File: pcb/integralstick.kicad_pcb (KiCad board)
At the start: 4 copper layers, 231 parts, among them J1 CONN_INTEGRALSTICK_FPGA_DEVICE, J2 CONN_INTEGRALSTICK_MCU_DEVICE, Q1 SSM6N58NU, Q2 SSM6N58NU, Q3 SSM6N58NU, U1 STM32F777NIH6‎, U10 DSC6083MI2A-032K768, U12 DSC6001HI2A-025.0000‎, U2 XC7A50T-1FTG256C, U3 S27KS0641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

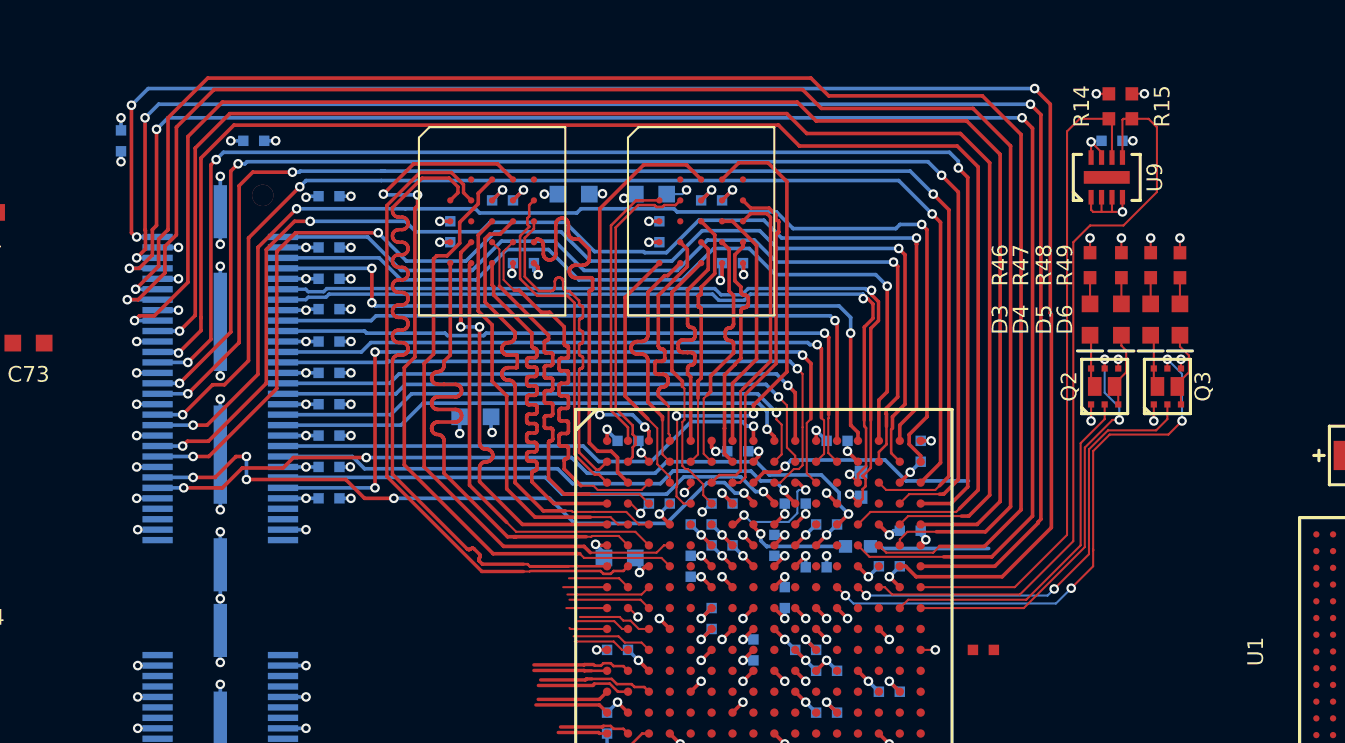
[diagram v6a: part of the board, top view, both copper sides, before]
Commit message: More efficient use of top right area above FPGA
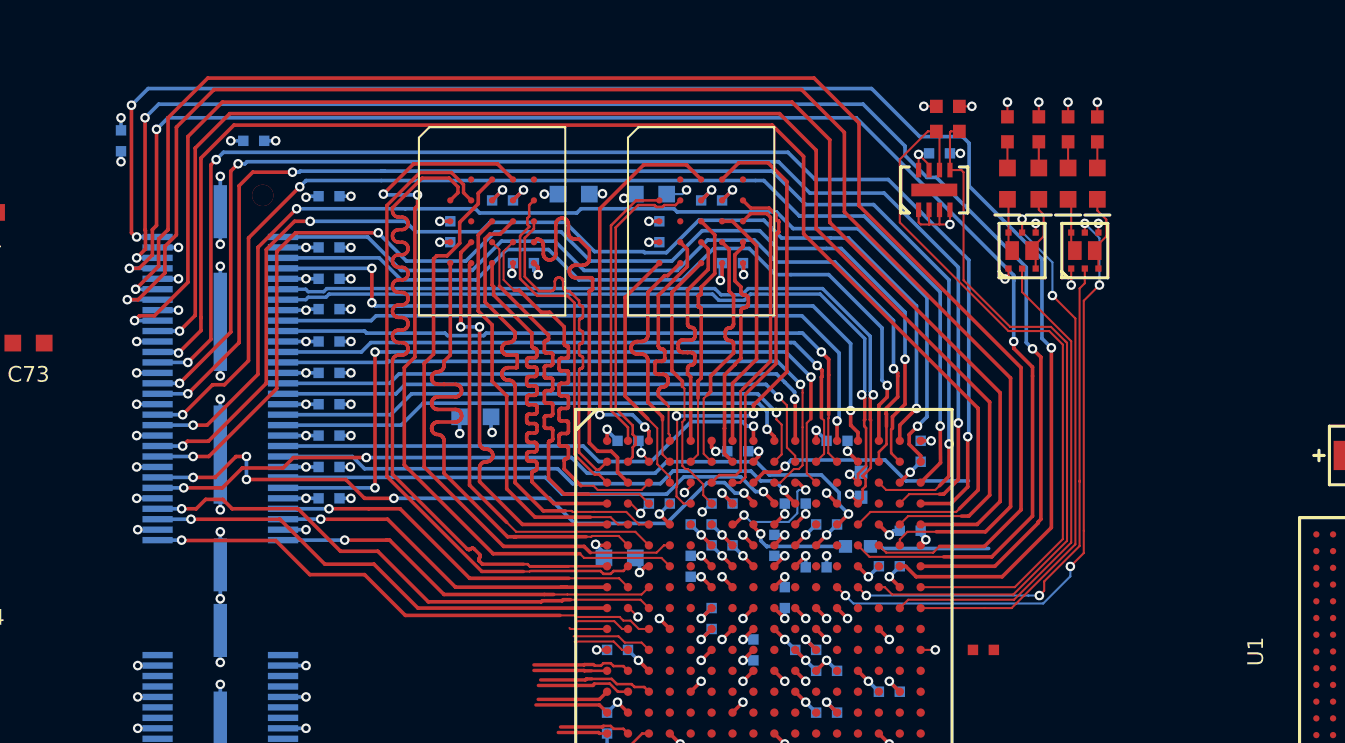
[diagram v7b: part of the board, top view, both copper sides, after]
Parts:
- moved C44 8.27 mm to (72.4, 21.8)
- moved R14 8.27 mm to (72.2, 20.1)
- moved R15 8.27 mm to (73.3, 20.1)
- moved U9 8.27 mm to (72.2, 23.5)
- moved D5 7.61 mm to (78.5, 23.2)
- moved D6 7.61 mm to (80.0, 23.2)
- moved Q2 7.61 mm to (76.3, 26.4)
- moved Q3 7.61 mm to (79.3, 26.4)
- moved R48 7.61 mm to (78.5, 20.6)
- moved R49 7.61 mm to (80.0, 20.6)
- moved D3 7.61 mm to (75.7, 23.2)
- moved D4 7.61 mm to (77.2, 23.2)
- moved R46 7.61 mm to (75.7, 20.6)
- moved R47 7.61 mm to (77.2, 20.6)
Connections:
- U2 pad E5: /RAM/GPIO_1V8_0 -> /RAM/GPIO_1V8_9
- U2 pad E6: /RAM/GPIO_1V8_1 -> /RAM/GPIO_1V8_7
- U2 pad G5: /RAM/GPIO_1V8_2 -> /RAM/GPIO_1V8_12
- U2 pad H1: /RAM/GPIO_1V8_8 -> /RAM/GPIO_1V8_3
- U2 pad H2: /RAM/GPIO_1V8_7 -> /RAM/GPIO_1V8_1
- U2 pad H3: /RAM/GPIO_1V8_10 -> /RAM/GPIO_1V8_5
- U2 pad H4: /RAM/GPIO_1V8_4 -> /RAM/GPIO_1V8_15
- U2 pad H5: /RAM/GPIO_1V8_3 -> /RAM/GPIO_1V8_8
- U2 pad J1: /RAM/GPIO_1V8_12 -> /RAM/GPIO_1V8_2
- U2 pad J3: /RAM/GPIO_1V8_9 -> /RAM/GPIO_1V8_0
- U2 pad J5: /RAM/GPIO_1V8_5 -> /RAM/GPIO_1V8_10
- U2 pad K3: /RAM/GPIO_1V8_15 -> /RAM/GPIO_1V8_4
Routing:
- net /RAM/GPIO_1V8_0: track 0.00 -> 26.0 mm, vias 0 -> 1
- net /RAM/GPIO_1V8_4: track 0.00 -> 25.3 mm, vias 0 -> 1
- net /RAM/GPIO_1V8_2: track 0.00 -> 23.3 mm, vias 0 -> 1
- net /RAM/GPIO_1V8_5: track 0.00 -> 18.7 mm, vias 0 -> 1
- net /RAM/GPIO_1V8_1: track 0.00 -> 18.1 mm, vias 0 -> 1
- net /RAM/GPIO_1V8_3: track 0.00 -> 17.1 mm, vias 0 -> 1
- net /FPGA/GPIO_LED0: track 17.1 -> 23.6 mm
- net /FPGA/GPIO_LED1: track 19.6 -> 25.9 mm
- net /FPGA/IO_3V3_25: track 79.1 -> 74.4 mm
- net /FPGA/IO_3V3_17: track 71.3 -> 66.7 mm
- net /FPGA/IO_3V3_19: track 70.5 -> 66.0 mm
- net /FPGA/IO_3V3_27: track 77.3 -> 72.8 mm
- net /FPGA/IO_3V3_21: track 72.8 -> 68.4 mm
- net /FPGA/IO_3V3_22: track 76.2 -> 71.9 mm
- net /FPGA/IO_3V3_23: track 78.3 -> 74.1 mm
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
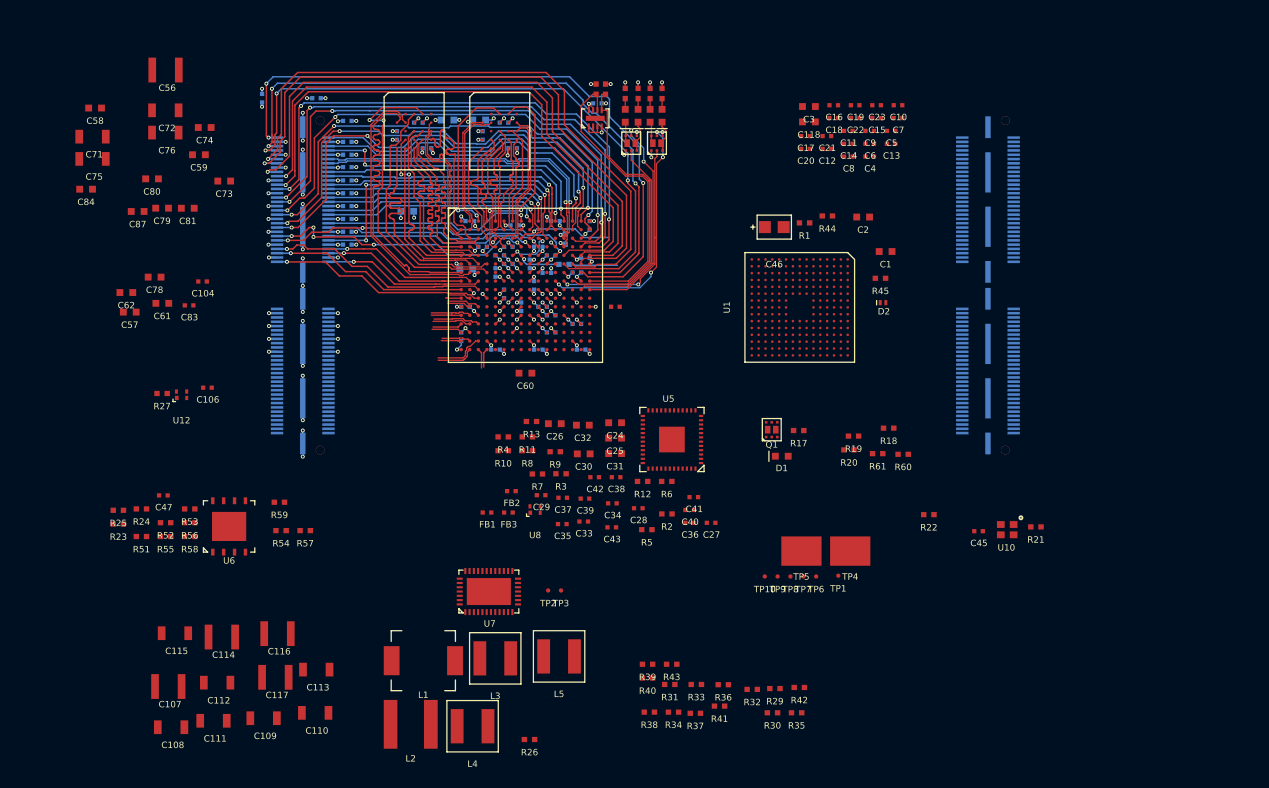
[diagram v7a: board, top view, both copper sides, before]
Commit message: Initial routing of LVCMOS18 GPIO bus. Hooked up a few 0603 decoupling caps.
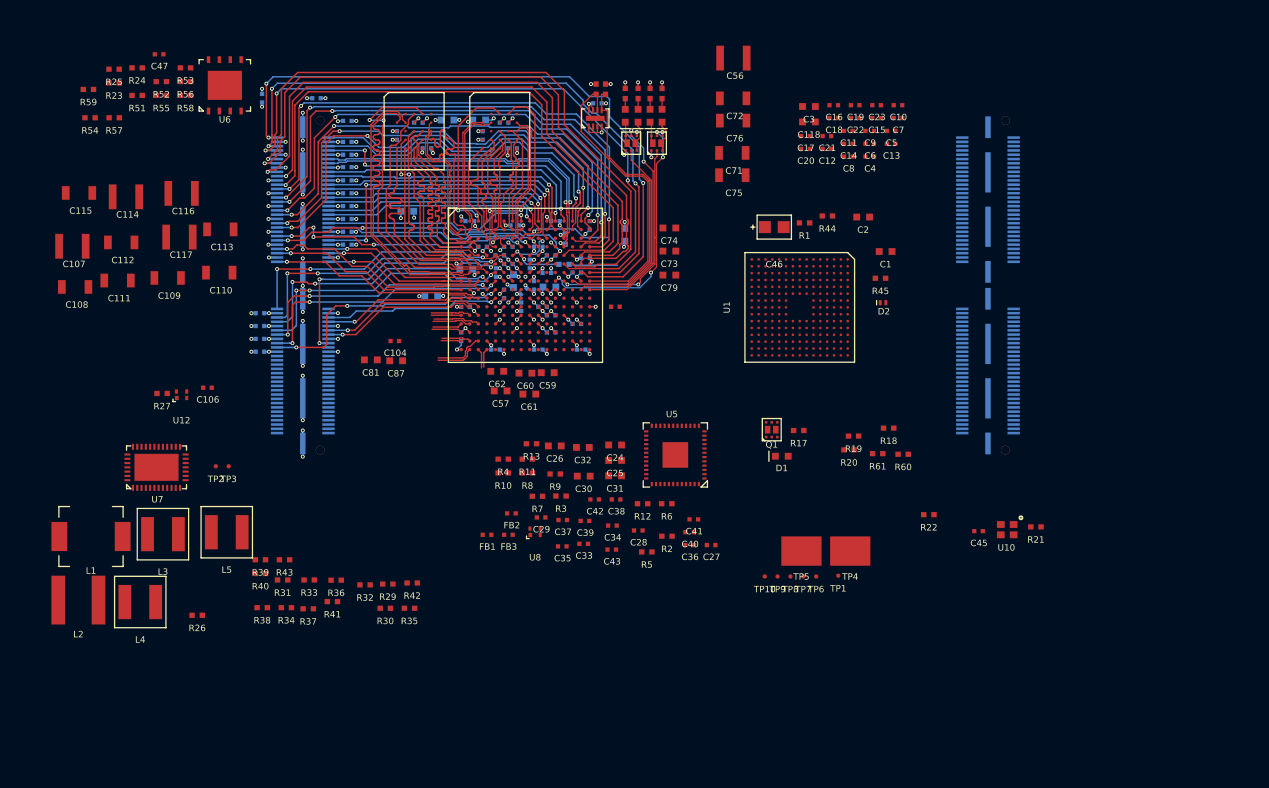
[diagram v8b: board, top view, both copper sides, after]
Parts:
- added C131: 0.47 uF, azonenberg_pcb:EIA_0402_CAP_NOSILK, B.Cu at (33.0, 49.2)
- added C132: 0.47 uF, azonenberg_pcb:EIA_0402_CAP_NOSILK, B.Cu at (33.0, 50.8)
- added C133: 0.47 uF, azonenberg_pcb:EIA_0402_CAP_NOSILK, B.Cu at (33.0, 46.2)
- added C134: 0.47 uF, azonenberg_pcb:EIA_0402_CAP_NOSILK, B.Cu at (33.0, 47.8)
- C58, C78, C80, C83, C84: moved to B.Cu
- moved C71 74.7 mm to (88.2, 27.5)
- moved C75 74.7 mm to (88.2, 30.1)
- moved C56 66.3 mm to (88.3, 16.4)
- moved C72 66.3 mm to (88.2, 21.2)
- moved C76 66.3 mm to (88.2, 23.8)
- moved C79 59.7 mm to (80.8, 41.8)
- moved C80 55.6 mm to (75.6, 37.1), turned to 90 degrees
- moved C74 55.5 mm to (80.8, 36.3)
- moved C84 55.3 mm to (66.8, 43.2)
- moved R54 53.1 mm to (13.2, 23.4)
- moved R57 53.1 mm to (16.0, 23.4)
- moved R59 53.1 mm to (13.0, 20.1)
- moved C58 52.9 mm to (62.6, 42.5), turned to 90 degrees
- moved C73 52.6 mm to (80.8, 39.0)
- moved C107 52.6 mm to (11.1, 38.4)
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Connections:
- J1 pad 41: /RAM/GPIO_1V8_16 -> /RAM/CLK_1V8_1
- J1 pad 42: /RAM/CLK_1V8_0 -> /RAM/GPIO_1V8_17
- J1 pad 43: /RAM/GPIO_1V8_17 -> /RAM/CLK_1V8_0
- J1 pad 44: /RAM/CLK_1V8_1 -> /RAM/GPIO_1V8_16
- U2 pad E5: /RAM/GPIO_1V8_9 -> /RAM/GPIO_1V8_6
- U2 pad E6: /RAM/GPIO_1V8_7 -> /RAM/GPIO_1V8_8
- U2 pad H4: /RAM/GPIO_1V8_15 -> /RAM/GPIO_1V8_10
- U2 pad H5: /RAM/GPIO_1V8_8 -> /RAM/GPIO_1V8_16
- U2 pad J4: /RAM/GPIO_1V8_6 -> /RAM/GPIO_1V8_14
- U2 pad J5: /RAM/GPIO_1V8_10 -> /RAM/GPIO_1V8_17
- U2 pad K2: /RAM/GPIO_1V8_16 -> /RAM/GPIO_1V8_7
- U2 pad K5: /RAM/GPIO_1V8_17 -> /RAM/GPIO_1V8_9
- U2 pad L2: /RAM/GPIO_1V8_14 -> /RAM/GPIO_1V8_15
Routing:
- net /RAM/GPIO_1V8_8: track 0.00 -> 33.1 mm, vias 0 -> 3
- net /RAM/GPIO_1V8_12: track 0.00 -> 31.5 mm, vias 0 -> 3
- net /RAM/GPIO_1V8_6: track 0.00 -> 31.4 mm, vias 0 -> 3
- net /RAM/CLK_1V8_0: track 0.00 -> 31.0 mm, vias 0 -> 3
- net /RAM/GPIO_1V8_10: track 0.00 -> 30.4 mm, vias 0 -> 3
- net /RAM/GPIO_1V8_17: track 0.00 -> 30.3 mm, vias 0 -> 3
- net /GND: track 355.0 -> 383.8 mm, vias 81 -> 89
- net /RAM/GPIO_1V8_16: track 2.58 -> 31.1 mm, vias 0 -> 3
- net /RAM/GPIO_1V8_14: track 2.72 -> 29.4 mm, vias 0 -> 3
- net /RAM/GPIO_1V8_9: track 0.00 -> 20.5 mm, vias 0 -> 1
- net /RAM/GPIO_1V8_15: track 0.00 -> 18.2 mm, vias 0 -> 1
- net /RAM/GPIO_1V8_13: track 3.87 -> 19.2 mm, vias 0 -> 1
- net /RAM/GPIO_1V8_11: track 1.82 -> 16.6 mm, vias 0 -> 1
- net /3V3: track 180.5 -> 170.8 mm, vias 43 -> 44
- net /1V8: track 158.5 -> 165.1 mm, vias 31 -> 32
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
